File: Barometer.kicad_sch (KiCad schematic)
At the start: 0 parts

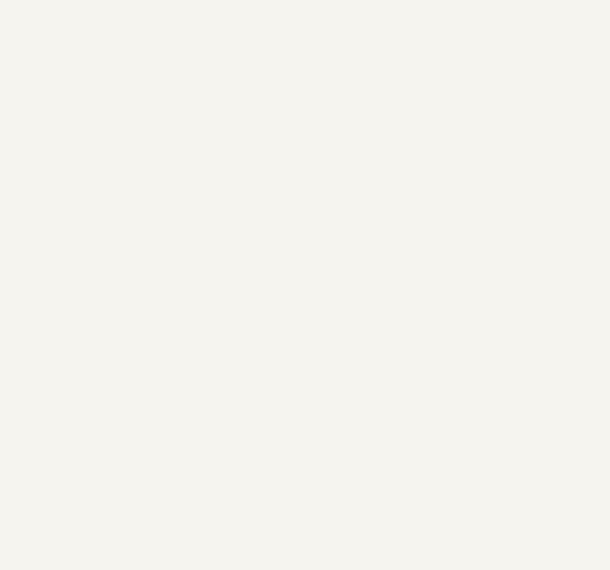
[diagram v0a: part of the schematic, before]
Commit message: added barometer schematic
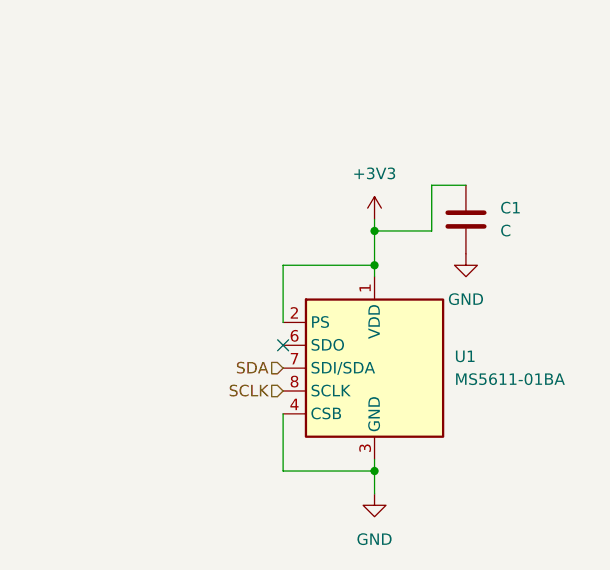
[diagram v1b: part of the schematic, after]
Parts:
- added C1: C, Package_LGA:LGA-8_3x5mm_P1.25mm, symbol Device:C
- added U1: MS5611-01BA, Package_LGA:LGA-8_3x5mm_P1.25mm, symbol Sensor_Pressure:MS5611-01BA
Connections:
- new net +3V3: C1.1, U1.1 (VDD), U1.2 (PS)
- new net GND: C1.2, U1.3 (GND), U1.4 (CSB), U1.5 (CSB)
- new net SCLK: U1.8 (SCLK)
- new net SDA: U1.7 (SDI/SDA)
- no-connect marks 0 -> 1
